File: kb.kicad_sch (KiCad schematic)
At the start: 182 parts, among them J1 Conn_01x04_Female, J2 10029449-001RLF, SW1 RotaryEncoder_Switch, U1 Pico, U2 SN74AHCT125D

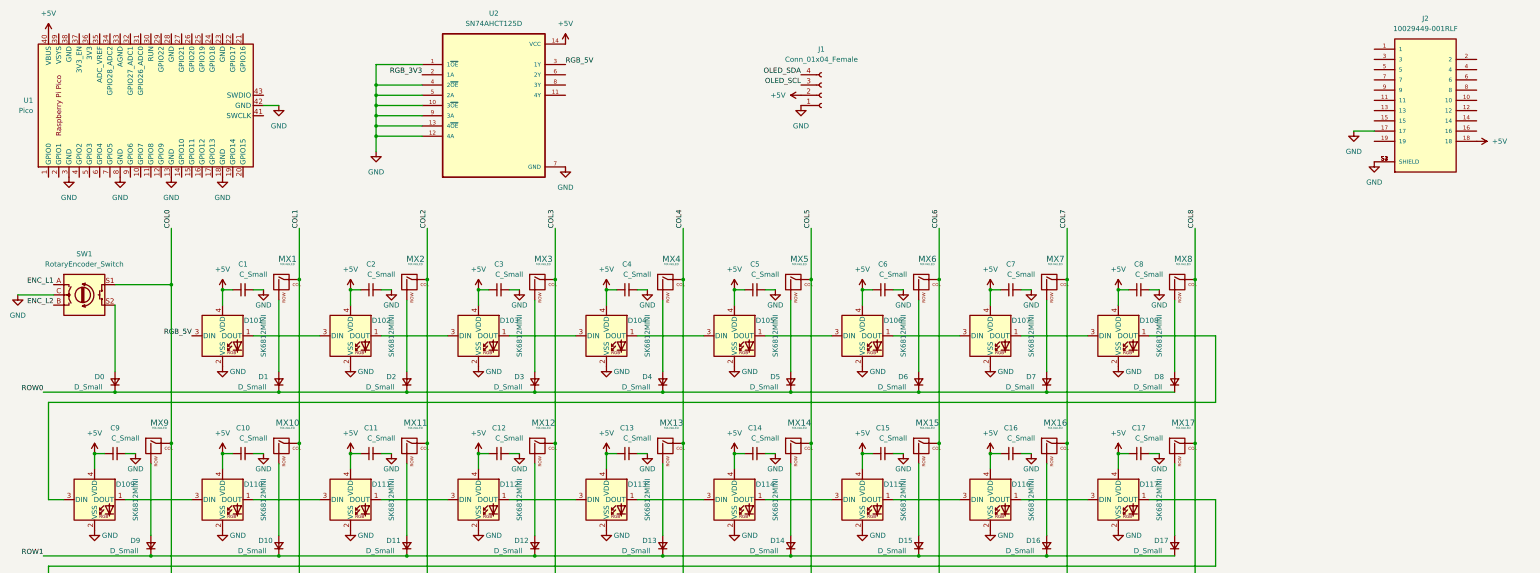
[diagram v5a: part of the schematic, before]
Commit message: cols 3-8 done
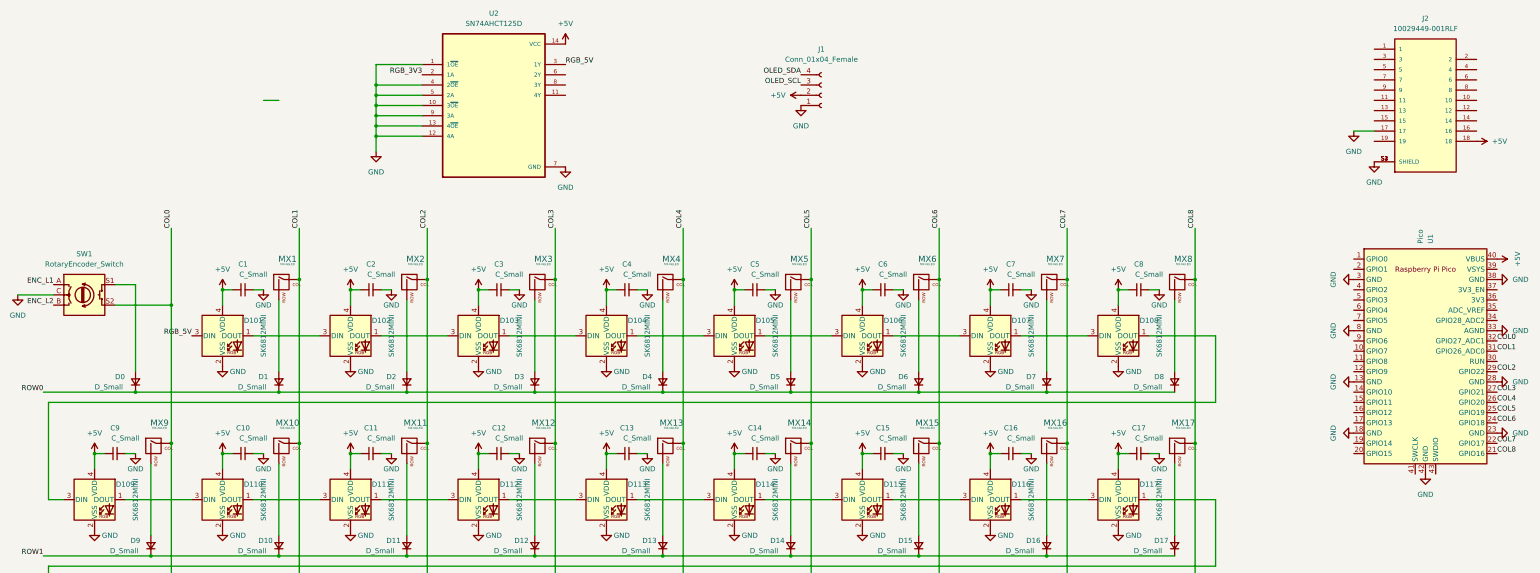
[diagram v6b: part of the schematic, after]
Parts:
- MX43: footprint MX_Only:MXOnly-2U-Hotswap -> MX_Only:MXOnly-2U-Hotswap-ReversedStabilizers
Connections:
- net COL0: now also SW1.S2, U1.32 (GPIO27_ADC1); no longer SW1.S1
- net COL1: now also U1.31 (GPIO26_ADC0)
- net COL2: now also U1.29 (GPIO22)
- net COL3: now also U1.27 (GPIO21)
- net COL4: now also U1.26 (GPIO20)
- net COL5: now also U1.25 (GPIO19)
- net COL6: now also U1.24 (GPIO18)
- net COL7: now also U1.22 (GPIO17)
- net COL8: now also U1.21 (GPIO16)
- net GND: now also U1.23 (GND), U1.28 (GND), U1.33 (AGND), U1.38 (GND)
- net at D0.2 (A): now also SW1.S1; no longer SW1.S2
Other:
- moved on the sheet: D0, U1

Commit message: before rgb restructure
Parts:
- removed C44: C_Small, Capacitor_SMD:C_0805_2012Metric_Pad1.18x1.45mm_HandSolder, symbol Device:C_Small
- removed D144: SK6812MINI, Keebio-Parts:SK6812-MINI-E, symbol LED:SK6812MINI
- added C?: C_Small, Capacitor_SMD:C_0805_2012Metric_Pad1.18x1.45mm_HandSolder, symbol Device:C_Small
- added D?: SK6812MINI, Keebio-Parts:SK6812-MINI-E, symbol LED:SK6812MINI
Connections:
- net +5V: now also C?.1, D?.4 (VDD); no longer J1.2 (Pin_2)
- net ENC_L1: now also U1.34 (GPIO28_ADC2)
- net ENC_L2: now also U1.1 (GPIO0)
- net GND: now also U2.2 (1A), C?.2, D?.2 (VSS); no longer U2.9 (3A)
- net OLED_SCL: now also U1.5 (GPIO3)
- net OLED_SDA: now also U1.4 (GPIO2)
- net RGB_3V3: now also U1.2 (GPIO1), U2.9 (3A); no longer U2.2 (1A)
- net RGB_5V: now also U2.8 (3Y); no longer U2.3 (1Y)
- net RGB_TO_RIGHT: now also D143.1 (DOUT), J2.19
- net at D109.3 (DIN): now also D?.1 (DOUT); no longer D108.1 (DOUT)
- net ENC_R1: now reaches J2.15
- net ENC_R1: now also U1.19 (GPIO14)
- net ENC_R2: now reaches J2.16
- net ENC_R2: now also U1.20 (GPIO15)
- net +3V3: now reaches U1.36 (3V3)
- net +3V3: now also J1.2 (Pin_2)
- new net: D108.1 (DOUT), D?.3 (DIN)
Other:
- moved on the sheet: U1

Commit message: relaying out?
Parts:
- gave numbers to parts that had none: 2
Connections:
- net COL0: now also U1.5 (GPIO3); no longer U1.32 (GPIO27_ADC1)
- net COL1: now also U1.9 (GPIO6); no longer U1.31 (GPIO26_ADC0)
- net COL2: now also U1.12 (GPIO9); no longer U1.29 (GPIO22)
- net COL3: now also U1.14 (GPIO10); no longer U1.27 (GPIO21)
- net COL4: now also U1.15 (GPIO11); no longer U1.26 (GPIO20)
- net COL5: now also U1.16 (GPIO12); no longer U1.25 (GPIO19)
- net COL6: now also U1.17 (GPIO13); no longer U1.24 (GPIO18)
- net COL7: now also U1.19 (GPIO14); no longer U1.22 (GPIO17)
- net COL8: now also U1.20 (GPIO15); no longer U1.21 (GPIO16)
- net ENC_L1: now also U1.1 (GPIO0); no longer U1.34 (GPIO28_ADC2)
- net ENC_L2: now also U1.2 (GPIO1); no longer U1.1 (GPIO0)
- net ENC_R1: now also U1.11 (GPIO8); no longer U1.19 (GPIO14)
- net ENC_R2: now also U1.10 (GPIO7); no longer U1.20 (GPIO15)
- net GND: no longer U1.42 (GND)
- net OLED_SCL: now also U1.7 (GPIO5); no longer U1.5 (GPIO3)
- net OLED_SDA: now also U1.6 (GPIO4); no longer U1.4 (GPIO2)
- net RGB_3V3: now also U1.4 (GPIO2); no longer U1.2 (GPIO1)
- net ROW0: now also U1.34 (GPIO28_ADC2)
- net ROW1: now also U1.32 (GPIO27_ADC1)
- net ROW2: now also U1.31 (GPIO26_ADC0)
- net ROW3: now also U1.29 (GPIO22)
- net ROW4: now also U1.27 (GPIO21)
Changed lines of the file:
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@@
     (stroke (width 0) (type default) (color 0 0 0 0))
   )
-  (label "COL5" (at 388.62 162.56 0)
-    (effects (font (size 1.27 1.27)) (justify left bottom))
-  )
-  (label "OLED_SDA" (at 353.06 132.08 180)
+  (label "RGB_3V3" (at 353.06 132.08 180)
     (effects (font (size 1.27 1.27)) (justify right bottom))
   )
-  (label "OLED_SCL" (at 353.06 134.62 180)
+  (label "COL5" (at 353.06 162.56 180)
     (effects (font (size 1.27 1.27)) (justify right bottom))
   )
@@
     (effects (font (size 1.27 1.27)) (justify right bottom))
   )
-  (label "ENC_R2" (at 353.06 172.72 180)
+  (label "ENC_R2" (at 353.06 147.32 180)
+    (effects (font (size 1.27 1.27)) (justify right bottom))
+  )
+  (label "COL2" (at 353.06 152.4 180)
+    (effects (font (size 1.27 1.27)) (justify right bottom))
+  )
+  (label "OLED_SDA" (at 353.06 137.16 180)
+    (effects (font (size 1.27 1.27)) (justify right bottom))
+  )
+  (label "COL4" (at 353.06 160.02 180)
     (effects (font (size 1.27 1.27)) (justify right bottom))
   )
@@
     (effects (font (size 1.27 1.27)) (justify left bottom))
   )
-  (label "COL4" (at 184.15 67.31 90)
+  (label "ROW3" (at 388.62 152.4 0)
+    (effects (font (size 1.27 1.27)) (justify left bottom))
+  )
+  (label "ROW1" (at 388.62 144.78 0)
     (effects (font (size 1.27 1.27)) (justify left bottom))
   )
-  (label "COL3" (at 388.62 157.48 0)
+  (label "COL4" (at 184.15 67.31 90)
     (effects (font (size 1.27 1.27)) (justify left bottom))
   )
+  (label "COL6" (at 353.06 165.1 180)
+    (effects (font (size 1.27 1.27)) (justify right bottom))
+  )
+  (label "COL0" (at 353.06 134.62 180)
+    (effects (font (size 1.27 1.27)) (justify right bottom))
+  )
   (label "COL1" (at 88.9 67.31 90)
     (effects (font (size 1.27 1.27)) (justify left bottom))
@@
     (effects (font (size 1.27 1.27)) (justify right bottom))
   )
-  (label "ROW0" (at 25.4 107.95 180)
+  (label "OLED_SCL" (at 353.06 139.7 180)
     (effects (font (size 1.27 1.27)) (justify right bottom))
   )
-  (label "ENC_L1" (at 388.62 139.7 0)
-    (effects (font (size 1.27 1.27)) (justify left bottom))
+  (label "ROW0" (at 25.4 107.95 180)
+    (effects (font (size 1.27 1.27)) (justify right bottom))
   )
   (label "RGB_TO_RIGHT" (at 355.6 45.72 180)
@@
     (effects (font (size 1.27 1.27)) (justify right bottom))
   )
-  (label "COL2" (at 388.62 152.4 0)
+  (label "COL3" (at 152.4 67.31 90)
     (effects (font (size 1.27 1.27)) (justify left bottom))
   )
-  (label "COL3" (at 152.4 67.31 90)
+  (label "ROW4" (at 388.62 157.48 0)
     (effects (font (size 1.27 1.27)) (justify left bottom))
   )
@@
     (effects (font (size 1.27 1.27)) (justify left bottom))
   )
+  (label "COL3" (at 353.06 157.48 180)
+    (effects (font (size 1.27 1.27)) (justify right bottom))
+  )
+  (label "COL7" (at 353.06 170.18 180)
+    (effects (font (size 1.27 1.27)) (justify right bottom))
+  )
   (label "COL0" (at 57.15 67.31 90)
     (effects (font (size 1.27 1.27)) (justify left bottom))
@@
     (effects (font (size 1.27 1.27)) (justify right bottom))
   )
-  (label "COL4" (at 388.62 160.02 0)
-    (effects (font (size 1.27 1.27)) (justify left bottom))
+  (label "ENC_L2" (at 353.06 127 180)
+    (effects (font (size 1.27 1.27)) (justify right bottom))
   )
   (label "ROW1" (at 25.4 148.59 180)
@@
     (effects (font (size 1.27 1.27)) (justify right bottom))
   )
-  (label "RGB_5V" (at 62.23 93.98 180)
+  (label "COL1" (at 353.06 144.78 180)
     (effects (font (size 1.27 1.27)) (justify right bottom))
   )
-  (label "COL0" (at 388.62 144.78 0)
-    (effects (font (size 1.27 1.27)) (justify left bottom))
-  )
-  (label "ENC_R1" (at 353.06 170.18 180)
+  (label "RGB_5V" (at 62.23 93.98 180)
     (effects (font (size 1.27 1.27)) (justify right bottom))
   )
-  (label "ENC_L2" (at 353.06 124.46 180)
+  (label "ENC_R1" (at 353.06 149.86 180)
     (effects (font (size 1.27 1.27)) (justify right bottom))
   )
-  (label "COL8" (at 388.62 172.72 0)
+  (label "ROW2" (at 388.62 147.32 0)
     (effects (font (size 1.27 1.27)) (justify left bottom))
   )
-  (label "COL6" (at 388.62 165.1 0)
-    (effects (font (size 1.27 1.27)) (justify left bottom))
-  )
-  (label "OLED_SCL" (at 213.36 31.75 180)
+  (label "ENC_L1" (at 353.06 124.46 180)
     (effects (font (size 1.27 1.27)) (justify right bottom))
   )
-  (label "RGB_3V3" (at 353.06 127 180)
+  (label "OLED_SCL" (at 213.36 31.75 180)
     (effects (font (size 1.27 1.27)) (justify right bottom))
   )
@@
     (effects (font (size 1.27 1.27)) (justify right bottom))
   )
+  (label "ROW0" (at 388.62 139.7 0)
+    (effects (font (size 1.27 1.27)) (justify left bottom))
+  )
   (label "RGB_5V" (at 154.94 31.75 0)
     (effects (font (size 1.27 1.27)) (justify left bottom))
@@
     (effects (font (size 1.27 1.27)) (justify right bottom))
   )
-  (label "COL1" (at 388.62 147.32 0)
-    (effects (font (size 1.27 1.27)) (justify left bottom))
-  )
-  (label "COL7" (at 388.62 170.18 0)
-    (effects (font (size 1.27 1.27)) (justify left bottom))
+  (label "COL8" (at 353.06 172.72 180)
+    (effects (font (size 1.27 1.27)) (justify right bottom))
   )
   (symbol (lib_id "Device:D_Small") (at 179.07 186.69 90) (unit 1)
@@
   (symbol (lib_id "LED:SK6812MINI") (at 330.2 93.98 0) (unit 1)
     (in_bom yes) (on_board yes)
-    (property "Reference" "D?" (id 0) (at 337.82 90.17 0))
+    (property "Reference" "D144" (id 0) (at 337.82 90.17 0))
     (property "Value" "SK6812MINI" (id 1) (at 340.36 93.98 90))
     (property "Footprint" "Keebio-Parts:SK6812-MINI-E" (id 2) (at 331.47 101.6 0)
@@
   (symbol (lib_id "power:+5V") (at 330.2 82.55 0) (unit 1)
     (in_bom yes) (on_board yes) (fields_autoplaced)
-    (property "Reference" "#PWR?" (id 0) (at 330.2 86.36 0)
+    (property "Reference" "#PWR0137" (id 0) (at 330.2 86.36 0)
       (effects (font (size 1.27 1.27)) hide)
     )
@@
   (symbol (lib_id "Device:C_Small") (at 335.28 82.55 90) (unit 1)
     (in_bom yes) (on_board yes)
-    (property "Reference" "C?" (id 0) (at 335.28 76.2 90))
+    (property "Reference" "C44" (id 0) (at 335.28 76.2 90))
     (property "Value" "C_Small" (id 1) (at 337.82 78.74 90))
     (property "Footprint" "Capacitor_SMD:C_0805_2012Metric_Pad1.18x1.45mm_HandSolder" (id 2) (at 335.28 82.55 0)
@@
     (pin "4")
     (pin "40")
-    (pin "41")
-    (pin "42")
-    (pin "43")
     (pin "5")
     (pin "6")
@@
   (symbol (lib_id "power:GND") (at 330.2 101.6 0) (unit 1)
     (in_bom yes) (on_board yes)
-    (property "Reference" "#PWR?" (id 0) (at 330.2 107.95 0)
+    (property "Reference" "#PWR0146" (id 0) (at 330.2 107.95 0)
       (effects (font (size 1.27 1.27)) hide)
     )
@@
     (pin "1")
   )
-  (symbol (lib_id "power:GND") (at 370.84 177.8 0) (unit 1)
-    (in_bom yes) (on_board yes) (fields_autoplaced)
-    (property "Reference" "#PWR05" (id 0) (at 370.84 184.15 0)
-      (effects (font (size 1.27 1.27)) hide)
-    )
-    (property "Value" "GND" (id 1) (at 370.84 182.88 0))
-    (property "Footprint" "" (id 2) (at 370.84 177.8 0)
-      (effects (font (size 1.27 1.27)) hide)
-    )
-    (property "Datasheet" "" (id 3) (at 370.84 177.8 0)
-      (effects (font (size 1.27 1.27)) hide)
-    )
-    (pin "1")
-  )
   (symbol (lib_id "Device:C_Small") (at 106.68 163.83 90) (unit 1)
     (in_bom yes) (on_board yes)
@@
   (symbol (lib_id "power:GND") (at 340.36 82.55 0) (unit 1)
     (in_bom yes) (on_board yes)
-    (property "Reference" "#PWR?" (id 0) (at 340.36 88.9 0)
+    (property "Reference" "#PWR0136" (id 0) (at 340.36 88.9 0)
       (effects (font (size 1.27 1.27)) hide)
     )
@@
       (reference "#PWR03") (unit 1) (value "+5V") (footprint "")
     )
-    (path "/ea285b07-cef3-4793-a9d5-b587e8978b14"
-      (reference "#PWR05") (unit 1) (value "GND") (footprint "")
-    )
     (path "/5942d04e-be6a-4578-aaa8-e090ca820f49"
       (reference "#PWR06") (unit 1) (value "GND") (footprint "")
@@
       (reference "#PWR0135") (unit 1) (value "GND") (footprint "")
     )
+    (path "/f6796264-7c3d-4773-9349-ab0aae6d944d"
+      (reference "#PWR0136") (unit 1) (value "GND") (footprint "")
+    )
+    (path "/5e220e0c-91e5-4b4c-8108-5e5196a78e74"
+      (reference "#PWR0137") (unit 1) (value "+5V") (footprint "")
+    )
     (path "/046b9c34-a429-4ae8-99f5-063aa677aae7"
       (reference "#PWR0138") (unit 1) (value "GND") (footprint "")
@@
       (reference "#PWR0145") (unit 1) (value "GND") (footprint "")
     )
+    (path "/aebd737e-ba5f-4039-bf73-d53c6e82355d"
+      (reference "#PWR0146") (unit 1) (value "GND") (footprint "")
+    )
     (path "/26a93ba2-09db-478c-9004-cf3fd247e76c"
       (reference "#PWR0147") (unit 1) (value "GND") (footprint "")
@@
       (reference "#PWR0153") (unit 1) (value "+3V3") (footprint "")
     )
-    (path "/5e220e0c-91e5-4b4c-8108-5e5196a78e74"
-      (reference "#PWR?") (unit 1) (value "+5V") (footprint "")
-    )
-    (path "/aebd737e-ba5f-4039-bf73-d53c6e82355d"
-      (reference "#PWR?") (unit 1) (value "GND") (footprint "")
-    )
-    (path "/f6796264-7c3d-4773-9349-ab0aae6d944d"
-      (reference "#PWR?") (unit 1) (value "GND") (footprint "")
-    )
     (path "/ebfcd835-8a5f-4fc3-90f5-2b09942c4133"
       (reference "C1") (unit 1) (value "C_Small") (footprint "Capacitor_SMD:C_0805_2012Metric_Pad1.18x1.45mm_HandSolder")
@@
     )
     (path "/88b98c82-e973-4eec-9756-cdc061ca06d4"
-      (reference "C?") (unit 1) (value "C_Small") (footprint "Capacitor_SMD:C_0805_2012Metric_Pad1.18x1.45mm_HandSolder")
+      (reference "C44") (unit 1) (value "C_Small") (footprint "Capacitor_SMD:C_0805_2012Metric_Pad1.18x1.45mm_HandSolder")
     )
     (path "/2d47f0f9-bde1-411f-b854-f8bdc11cfcb5"
@@
     )
     (path "/15f88a7d-ebdd-45c8-946d-516a01984c19"
-      (reference "D?") (unit 1) (value "SK6812MINI") (footprint "Keebio-Parts:SK6812-MINI-E")
+      (reference "D144") (unit 1) (value "SK6812MINI") (footprint "Keebio-Parts:SK6812-MINI-E")
     )
     (path "/43ad0d80-cf3d-4fbe-b500-f317ef4293be"
